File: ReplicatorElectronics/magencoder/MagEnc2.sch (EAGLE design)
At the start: 13 parts, among them J1 SBH11-PBPC-D07-ST-BK, J2 70553-0037, T1 MMBT2222A

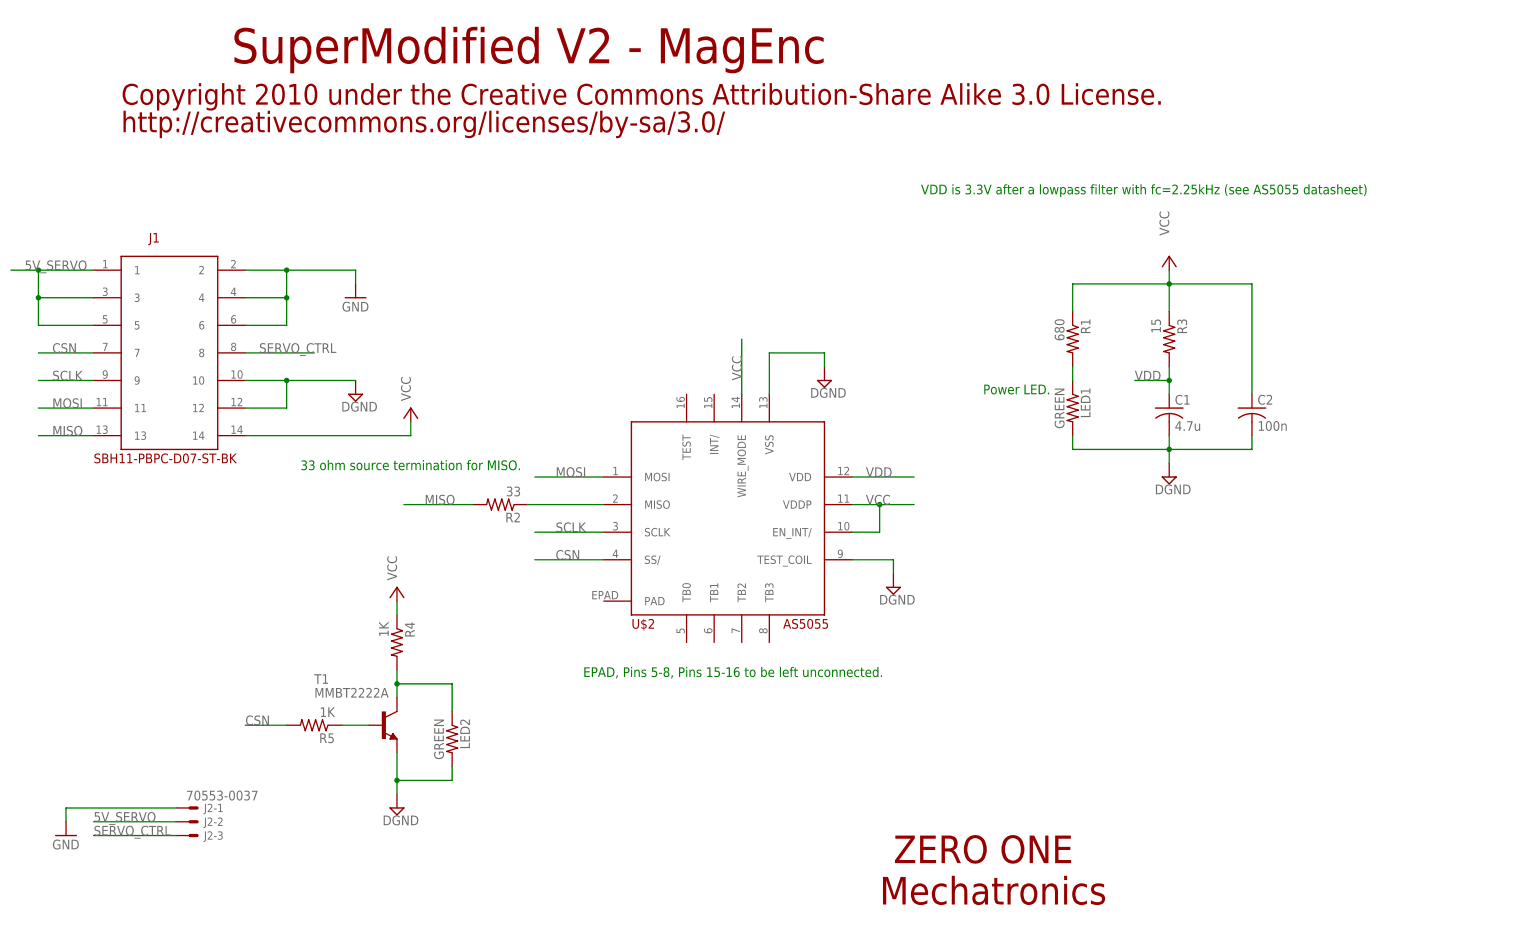
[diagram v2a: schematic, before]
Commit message: 2/10/13: Updated Encoder Board to include level translation. ~1 hour
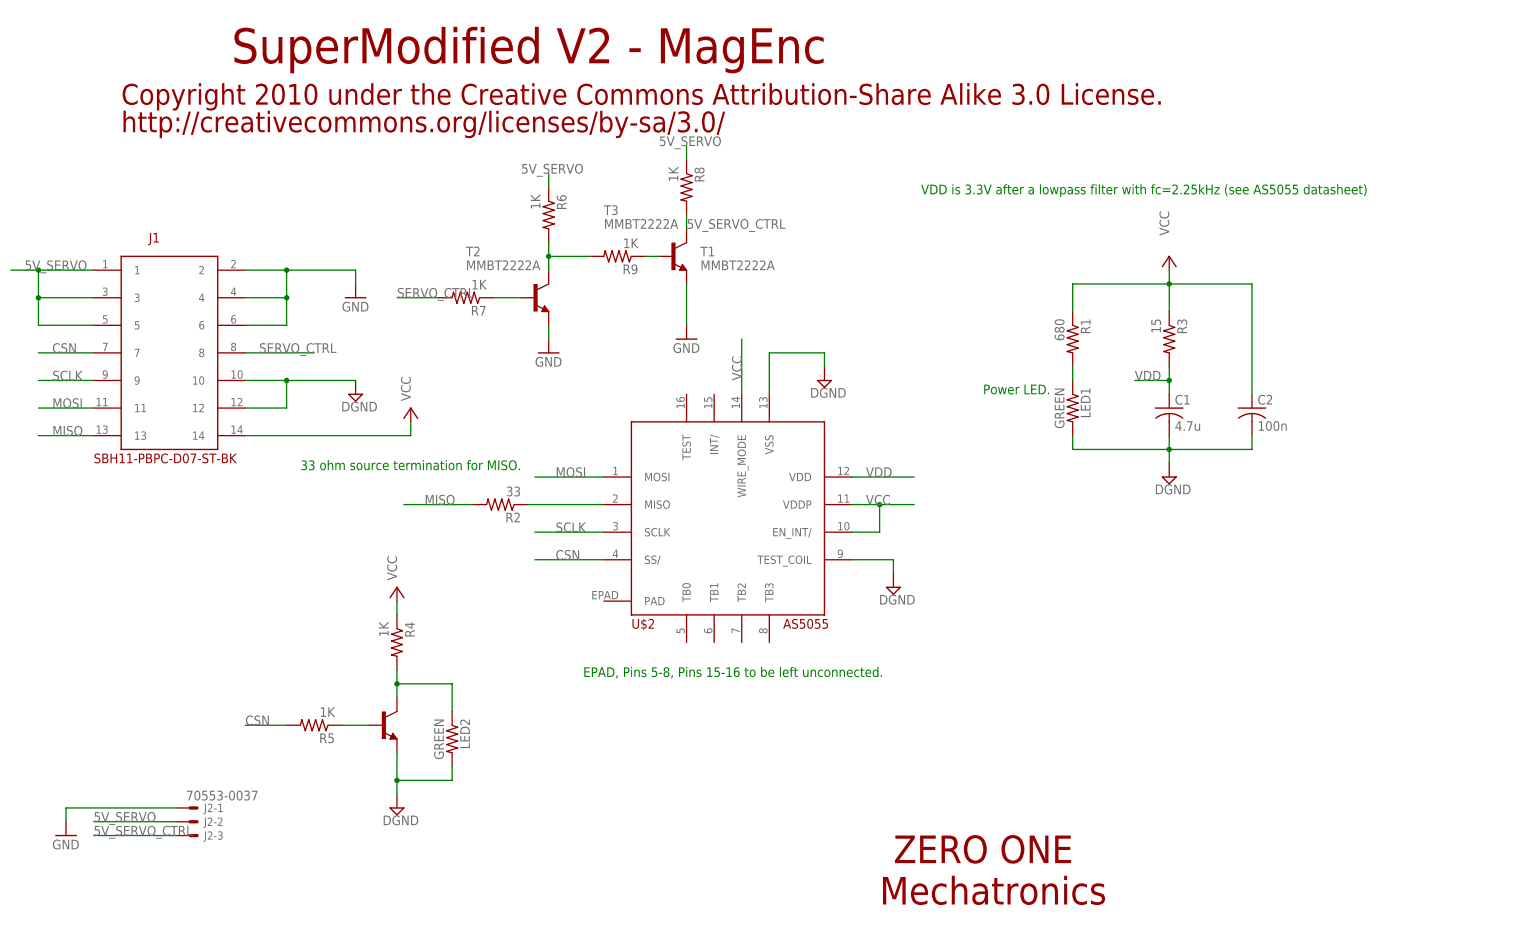
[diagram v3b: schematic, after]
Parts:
- added R6, R7, R8, R9: 1K, resistor:R-US_R0402
- added T2, T3: MMBT2222A, transistor:MMBT2222ALT1-NPN-SOT23-BEC
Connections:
- new net 5V_SERVO_CTRL: J2-3.S, R8.2, T3.C
- new net CSN1: R6.2, R9.2, T2.C
- new net N$6: R7.1, T2.B
- new net N$8: R9.1, T3.B
- net 5V_SERVO: now also R6.1, R8.1
- net GND: now also T2.E, T3.E
- net SERVO_CTRL: now also R7.2; no longer J2-3.S
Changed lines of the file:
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@@
 <?xml version="1.0" encoding="utf-8"?>
 <!DOCTYPE eagle SYSTEM "eagle.dtd">
-<eagle version="6.2">
+<eagle version="6.1">
 <drawing>
 <settings>
@@
 <part name="LED2" library="resistor" deviceset="R-US_" device="R0402" value="GREEN"/>
 <part name="LED1" library="resistor" deviceset="R-US_" device="R0402" value="GREEN"/>
+<part name="T2" library="transistor" deviceset="*-NPN-" device="SOT23-BEC" technology="MMBT2222ALT1" value="MMBT2222A"/>
+<part name="R6" library="resistor" deviceset="R-US_" device="R0402" value="1K"/>
+<part name="R7" library="resistor" deviceset="R-US_" device="R0402" value="1K"/>
+<part name="T3" library="transistor" deviceset="*-NPN-" device="SOT23-BEC" technology="MMBT2222ALT1" value="MMBT2222A"/>
+<part name="R8" library="resistor" deviceset="R-US_" device="R0402" value="1K"/>
+<part name="R9" library="resistor" deviceset="R-US_" device="R0402" value="1K"/>
+<part name="GND2" library="supply1" deviceset="GND" device=""/>
+<part name="GND3" library="supply1" deviceset="GND" device=""/>
 </parts>
 <sheets>
@@
 <instance part="J1" gate="G$1" x="-68.58" y="53.34"/>
 <instance part="T1" gate="G$1" x="-22.86" y="-15.24" smashed="yes">
-<attribute name="NAME" x="-35.56" y="-7.62" size="1.778" layer="95"/>
-<attribute name="VALUE" x="-35.56" y="-10.16" size="1.778" layer="96"/>
+<attribute name="NAME" x="35.56" y="71.12" size="1.778" layer="95"/>
+<attribute name="VALUE" x="35.56" y="68.58" size="1.778" layer="96"/>
 </instance>
 <instance part="R4" gate="G$1" x="-20.32" y="0" rot="R270"/>
@@
 <instance part="LED2" gate="G$1" x="-10.16" y="-17.78" rot="R270"/>
 <instance part="LED1" gate="G$1" x="104.14" y="43.18" rot="R270"/>
+<instance part="T2" gate="G$1" x="5.08" y="63.5" smashed="yes">
+<attribute name="NAME" x="-7.62" y="71.12" size="1.778" layer="95"/>
+<attribute name="VALUE" x="-7.62" y="68.58" size="1.778" layer="96"/>
+</instance>
+<instance part="R6" gate="G$1" x="7.62" y="78.74" rot="R270"/>
+<instance part="R7" gate="G$1" x="-7.62" y="63.5" rot="R180"/>
+<instance part="T3" gate="G$1" x="30.48" y="71.12" smashed="yes">
+<attribute name="NAME" x="17.78" y="78.74" size="1.778" layer="95"/>
+<attribute name="VALUE" x="17.78" y="76.2" size="1.778" layer="96"/>
+</instance>
+<instance part="R8" gate="G$1" x="33.02" y="83.82" rot="R270"/>
+<instance part="R9" gate="G$1" x="20.32" y="71.12" rot="R180"/>
+<instance part="GND2" gate="1" x="7.62" y="53.34"/>
+<instance part="GND3" gate="1" x="33.02" y="55.88"/>
 </instances>
 <busses>
@@
 <wire x1="-81.28" y1="-30.48" x2="-60.96" y2="-30.48" width="0.1524" layer="91"/>
 </segment>
+<segment>
+<pinref part="T2" gate="G$1" pin="E"/>
+<wire x1="7.62" y1="58.42" x2="7.62" y2="55.88" width="0.1524" layer="91"/>
+<pinref part="GND2" gate="1" pin="GND"/>
+</segment>
+<segment>
+<pinref part="T3" gate="G$1" pin="E"/>
+<wire x1="33.02" y1="66.04" x2="33.02" y2="58.42" width="0.1524" layer="91"/>
+<pinref part="GND3" gate="1" pin="GND"/>
+</segment>
 </net>
 <net name="VCC" class="0">
@@
 <label x="-76.2" y="-33.02" size="1.778" layer="95"/>
 </segment>
+<segment>
+<pinref part="R6" gate="G$1" pin="1"/>
+<wire x1="7.62" y1="86.36" x2="7.62" y2="83.82" width="0.1524" layer="91"/>
+<label x="2.54" y="86.36" size="1.778" layer="95"/>
+</segment>
+<segment>
+<pinref part="R8" gate="G$1" pin="1"/>
+<wire x1="33.02" y1="91.44" x2="33.02" y2="88.9" width="0.1524" layer="91"/>
+<label x="27.94" y="91.44" size="1.778" layer="95"/>
+</segment>
 </net>
 <net name="SERVO_CTRL" class="0">
@@
 </segment>
 <segment>
-<pinref part="J2" gate="-3" pin="S"/>
-<wire x1="-60.96" y1="-35.56" x2="-76.2" y2="-35.56" width="0.1524" layer="91"/>
-<label x="-76.2" y="-35.56" size="1.778" layer="95"/>
+<pinref part="R7" gate="G$1" pin="2"/>
+<wire x1="-12.7" y1="63.5" x2="-20.32" y2="63.5" width="0.1524" layer="91"/>
+<label x="-20.32" y="63.5" size="1.778" layer="95"/>
 </segment>
 </net>
@@
 </segment>
 </net>
+<net name="N$6" class="0">
+<segment>
+<pinref part="T2" gate="G$1" pin="B"/>
+<wire x1="2.54" y1="63.5" x2="-2.54" y2="63.5" width="0.1524" layer="91"/>
+<pinref part="R7" gate="G$1" pin="1"/>
+</segment>
+</net>
+<net name="CSN1" class="0">
+<segment>
+<pinref part="R9" gate="G$1" pin="2"/>
+<wire x1="15.24" y1="71.12" x2="7.62" y2="71.12" width="0.1524" layer="91"/>
+<pinref part="T2" gate="G$1" pin="C"/>
+<pinref part="R6" gate="G$1" pin="2"/>
+<wire x1="7.62" y1="68.58" x2="7.62" y2="71.12" width="0.1524" layer="91"/>
+<wire x1="7.62" y1="71.12" x2="7.62" y2="73.66" width="0.1524" layer="91"/>
+<junction x="7.62" y="71.12"/>
+</segment>
+</net>
+<net name="5V_SERVO_CTRL" class="0">
+<segment>
+<pinref part="T3" gate="G$1" pin="C"/>
+<pinref part="R8" gate="G$1" pin="2"/>
+<wire x1="33.02" y1="76.2" x2="33.02" y2="78.74" width="0.1524" layer="91"/>
+<label x="33.02" y="76.2" size="1.778" layer="95"/>
+</segment>
+<segment>
+<pinref part="J2" gate="-3" pin="S"/>
+<wire x1="-60.96" y1="-35.56" x2="-76.2" y2="-35.56" width="0.1524" layer="91"/>
+<label x="-76.2" y="-35.56" size="1.778" layer="95"/>
+</segment>
+</net>
+<net name="N$8" class="0">
+<segment>
+<pinref part="T3" gate="G$1" pin="B"/>
+<wire x1="27.94" y1="71.12" x2="25.4" y2="71.12" width="0.1524" layer="91"/>
+<pinref part="R9" gate="G$1" pin="1"/>
+</segment>
+</net>
